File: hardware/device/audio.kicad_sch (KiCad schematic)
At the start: 32 parts, among them J5 AUDIO_MODULE, J6 LINE_IN, J7 LINE_OUT, U24 WM8904CGEFL/RV, U28 TPS560200

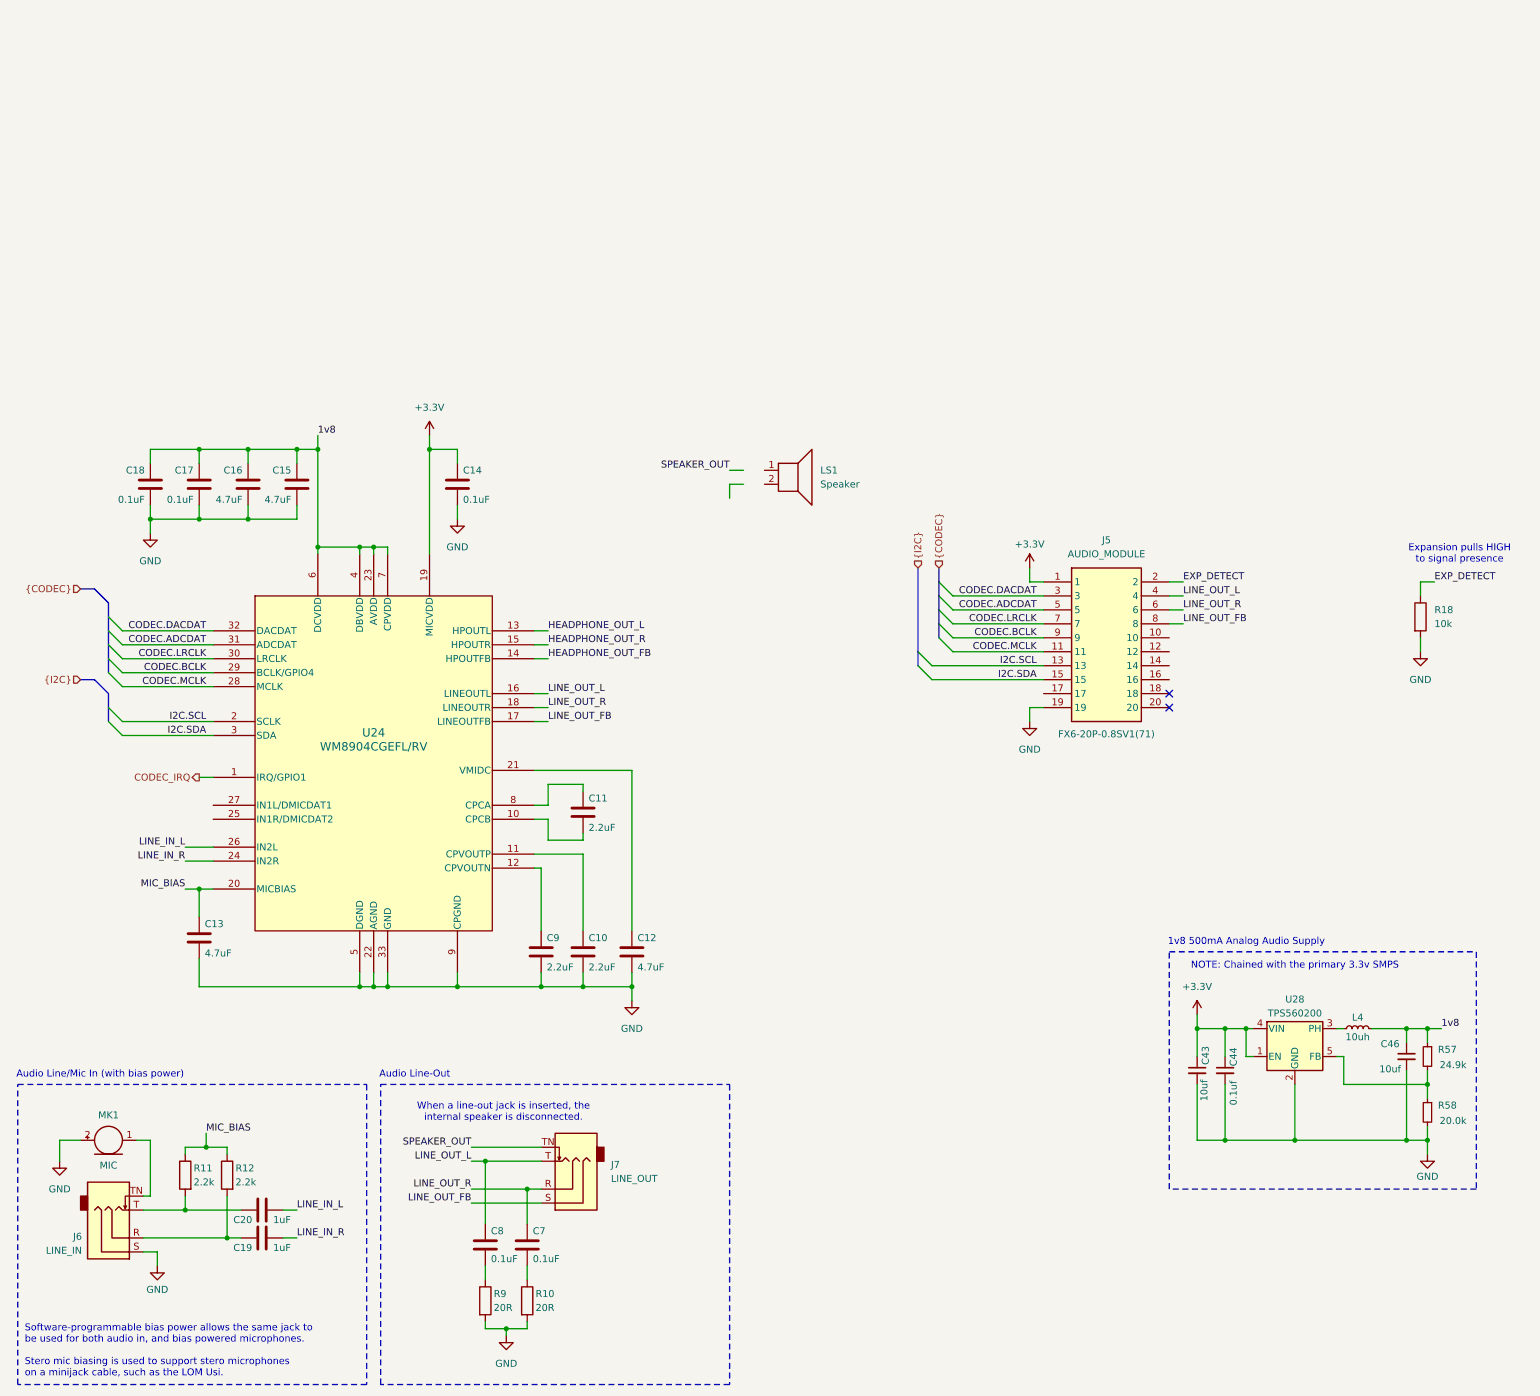
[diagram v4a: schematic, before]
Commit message: feat: speaker amplifier setup
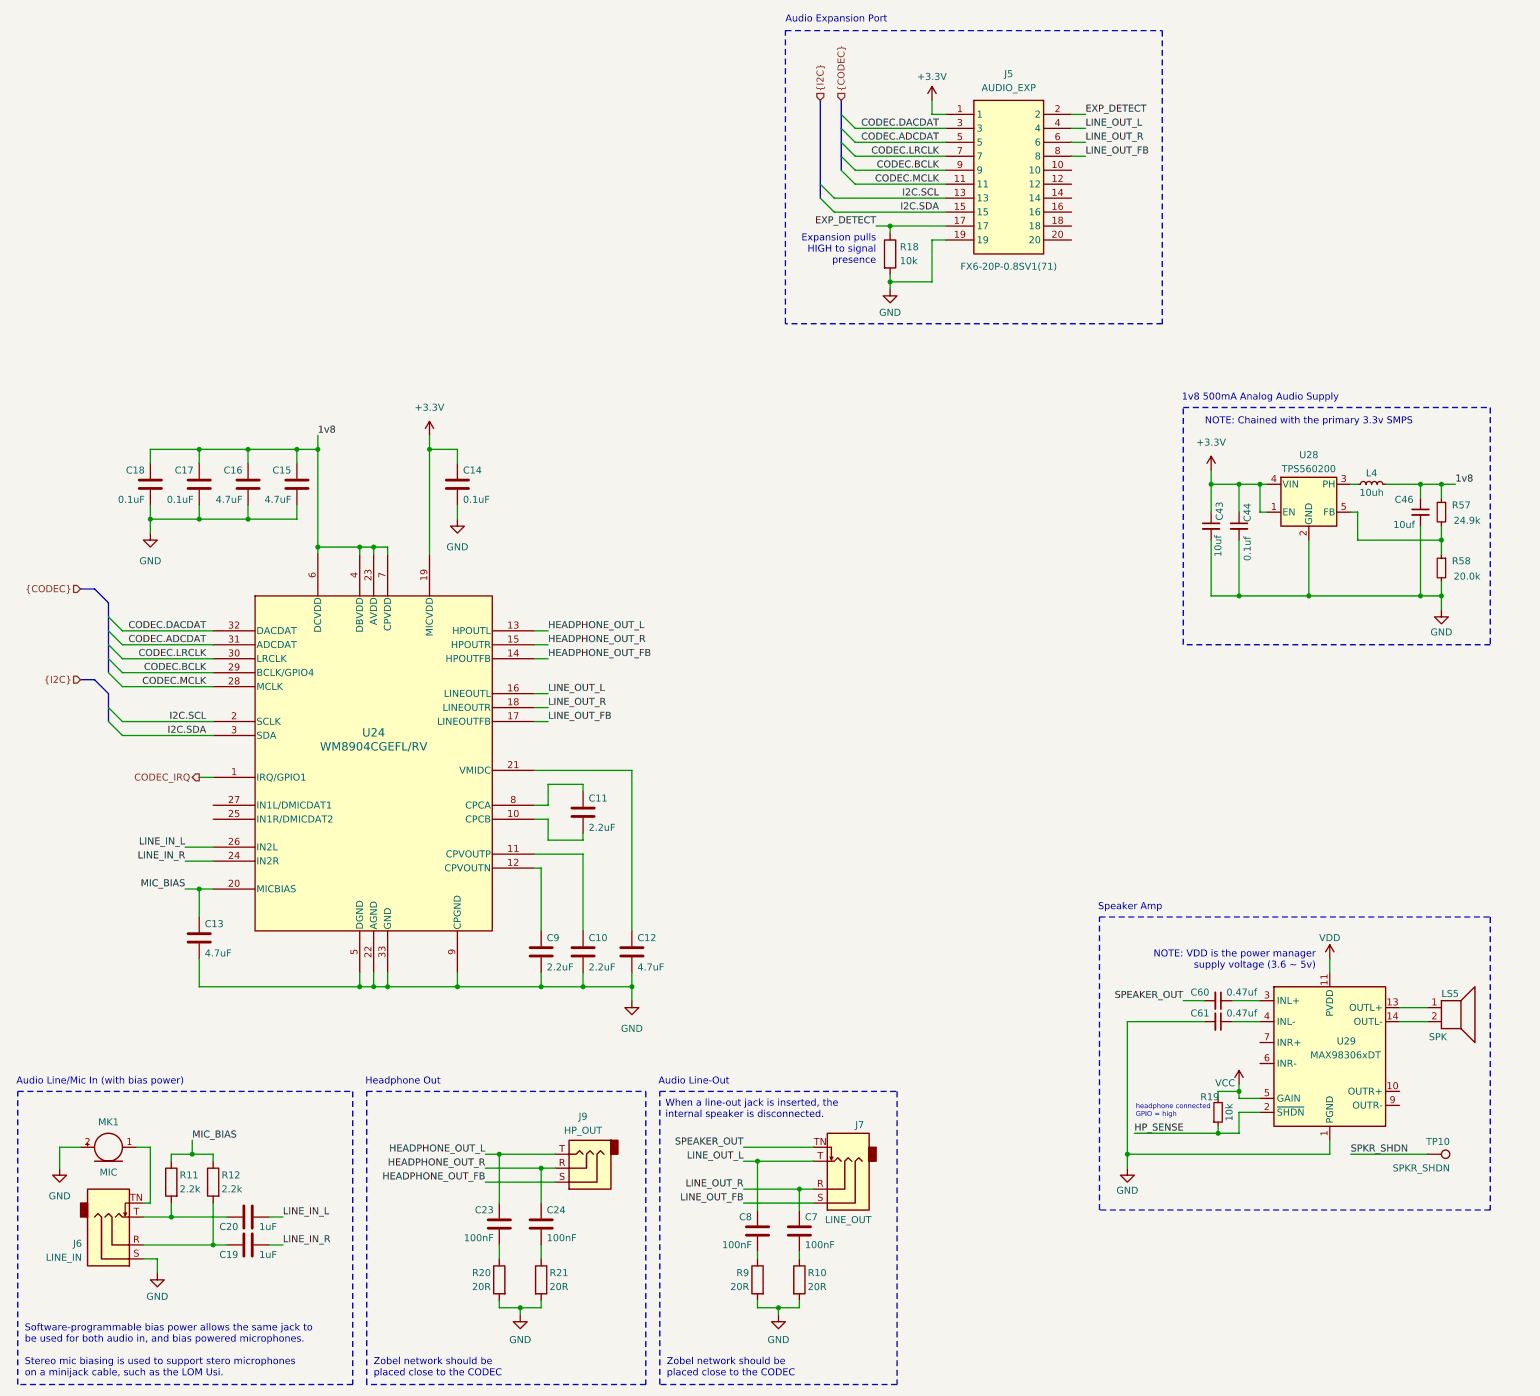
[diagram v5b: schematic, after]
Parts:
- removed LS1: Speaker, symbol Device:Speaker
- added C23, C24: 100nF, Capacitor_SMD:C_0402_1005Metric_Pad0.74x0.62mm_HandSolder, symbol Device:C
- added C60, C61: 0.47uf, symbol Device:C_Small
- added J9: HP_OUT, Connector_Audio:Jack_3.5mm_CUI_SJ-3523-SMT_Horizontal, symbol Connector_Audio:AudioJack3
- added LS5: SPK, symbol Device:Speaker
- added R19: 10k, symbol Device:R_Small
- added R20, R21: 20R, Resistor_SMD:R_0402_1005Metric_Pad0.72x0.64mm_HandSolder, symbol Device:R
- added TP10: SPKR_SHDN, TestPoint:TestPoint_Pad_D2.5mm, symbol Connector:TestPoint
- added U29: MAX98306xDT, Package_DFN_QFN:TDFN-14-1EP_3x3mm_P0.4mm_EP1.78x2.35mm, symbol Amplifier_Audio:MAX98306xDT
- C7, C8: value 0.1uF -> 100nF
- J5: value AUDIO_MODULE -> AUDIO_EXP
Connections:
- net EXP_DETECT: now also J5.17
- net GND: now also C61.2, R20.2, R21.2, U29.1 (PGND), U29.15 (PGND), U29.8 (PGND)
- net HEADPHONE_OUT_FB: now also J9.S
- net HEADPHONE_OUT_L: now also C23.1, J9.T
- net HEADPHONE_OUT_R: now also C24.1, J9.R
- net SPEAKER_OUT: now also C60.2
- new net: C60.1, U29.3 (INL+)
- new net: C24.2, R21.1
- new net: C61.1, U29.4 (INL-)
- new net: LS5.1, U29.13 (OUTL+)
- new net: LS5.2, U29.14 (OUTL-)
- new net: C23.2, R20.1
- new net HP_SENSE: R19.1, U29.2 (~{SHDN})
- new net SPKR_SHDN: TP10.1
- new net VCC: R19.2, U29.5 (GAIN)
- new net VDD: U29.11 (PVDD), U29.12 (PVDD)
- no-connect marks 2 -> 0
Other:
- note added: "Audio Expansion Port"
- note added: "Headphone Out"
- note added: "NOTE: VDD is the power manager supply voltage (3.6 ~ 5v)"
- note added: "Software-programmable bias power allows the same jack to be used for both audio in, and bias powered microphones. Stereo mic biasing is used to support stero microphones on a minijack cable, such as the LOM Usi."
- note added: "Speaker Amp"
- note added: "Zobel network should be placed close to the CODEC"
- note added: "headphone connected GPIO = high"
- note removed: "Software-programmable bias power allows the same jack to be used for both audio in, and bias powered microphones. Stero mic biasing is used to support stero microphones on a minijack cable, such as the LOM Usi."
- moved on the sheet: C19, C20, C43, C44, C46, C7, C8, J5, J6, J7, L4, MK1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

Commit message: feat: audio system layout
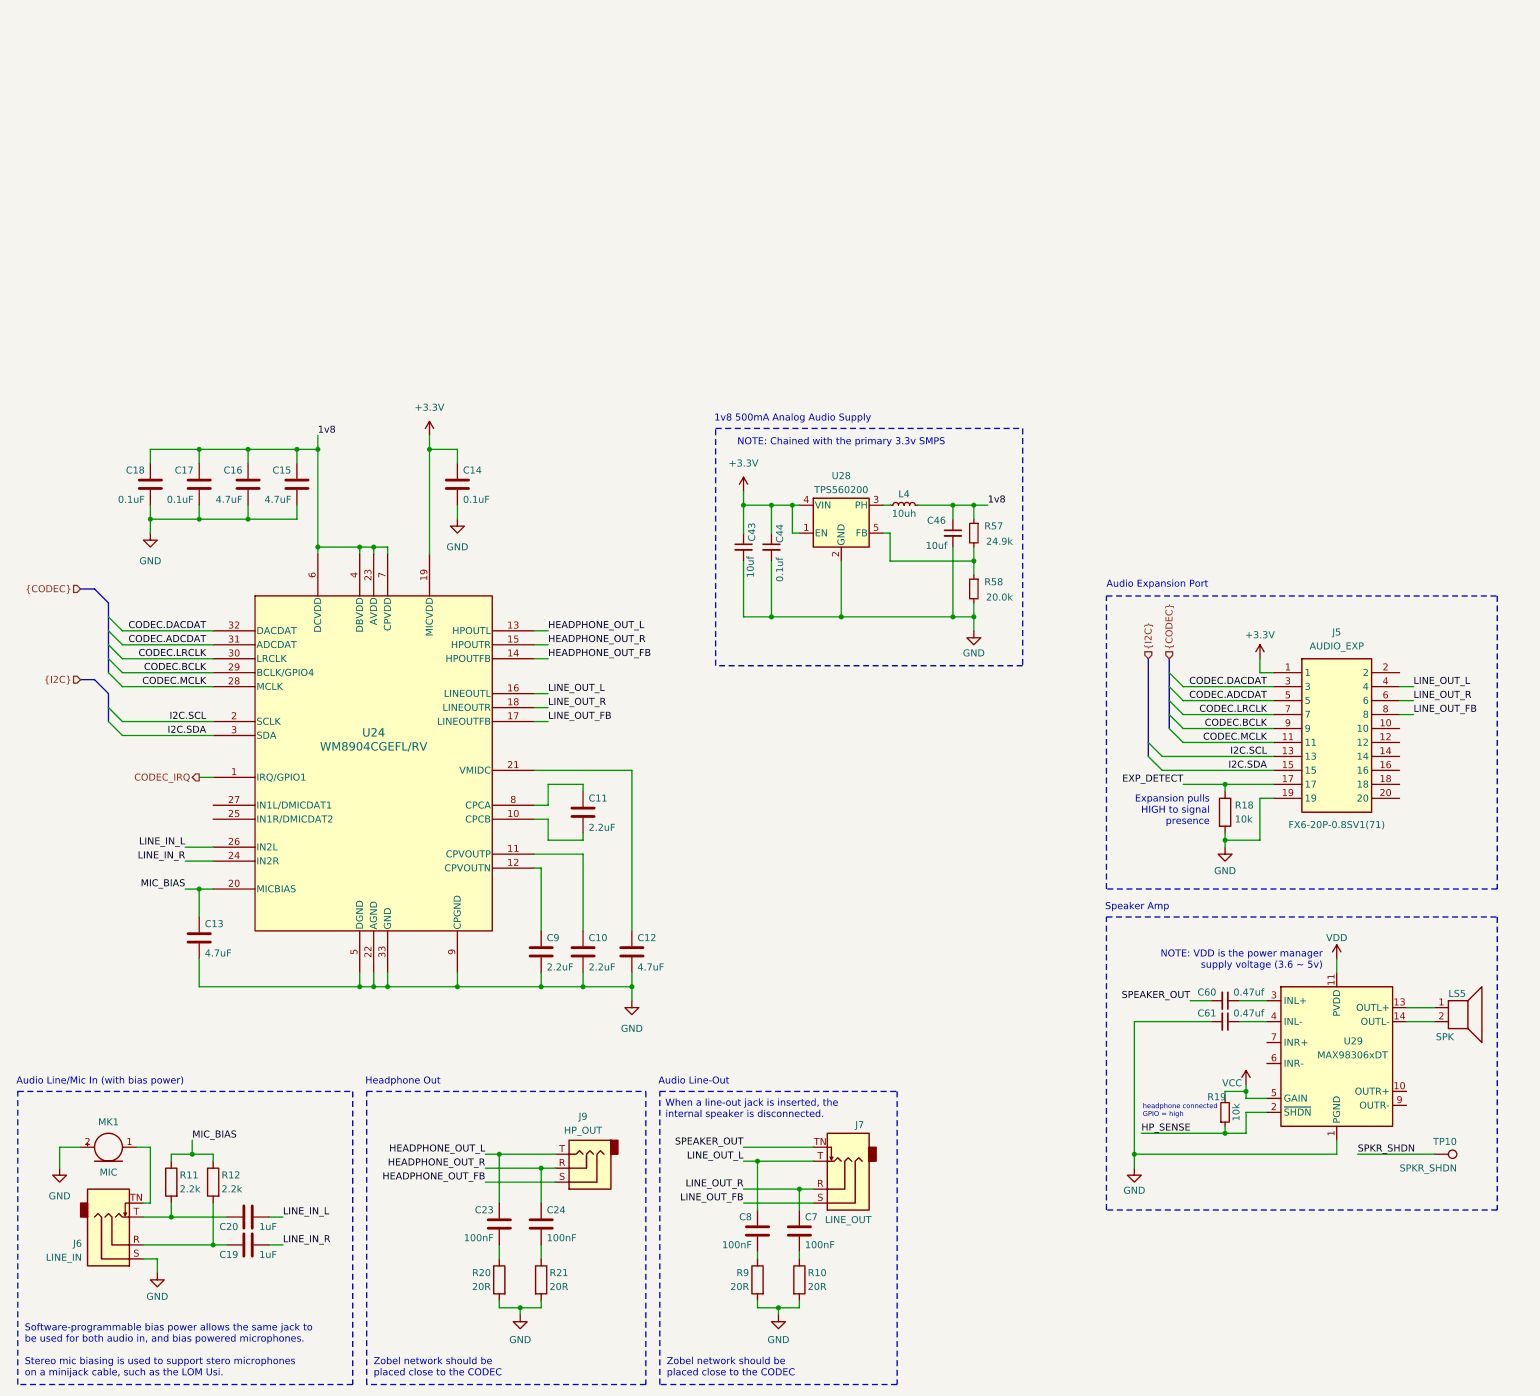
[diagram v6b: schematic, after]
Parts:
- C10, C11, C12, C13, C14, C15, C16, C17, C18, C19, C20, C23, C24, C43, C44, C46, C7, C8, C9: footprint Capacitor_SMD:C_0402_1005Metric_Pad0.74x0.62mm_HandSolder -> Capacitor_SMD:C_0201_0603Metric
- C60, C61: footprint (none) -> Capacitor_SMD:C_0201_0603Metric
- R10, R20, R21, R9: footprint Resistor_SMD:R_0402_1005Metric_Pad0.72x0.64mm_HandSolder -> Resistor_SMD:R_0201_0603Metric
- R11, R12, R57, R58: footprint Capacitor_SMD:C_0402_1005Metric_Pad0.74x0.62mm_HandSolder -> Resistor_SMD:R_0201_0603Metric
- R18, R19: footprint (none) -> Resistor_SMD:R_0201_0603Metric
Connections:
- net EXP_DETECT: no longer J5.2
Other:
- moved on the sheet: C43, C44, C46, C60, C61, J5, L4, LS5, R18, R19, R57, R58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
